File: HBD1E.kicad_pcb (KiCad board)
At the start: 2 copper layers, 73.1 x 50 mm, 62 parts, among them J1 Conn_01x08_Male, Q1 C3M0030090K, Q2 C3M0030090K, U1 UCC21520DW, U2 LM317_SOT-223, U3 3S7B-2424S3UP, U4 LM317_SOT-223, U5 3S7B-2424S3UP

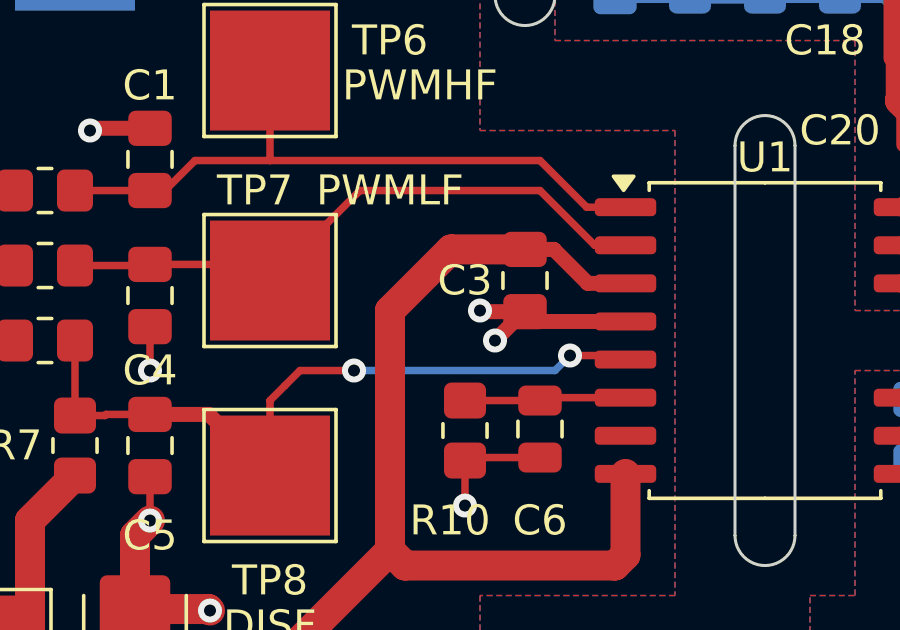
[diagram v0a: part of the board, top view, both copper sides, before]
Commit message: Added a pull-up resistor for dead time configuration.
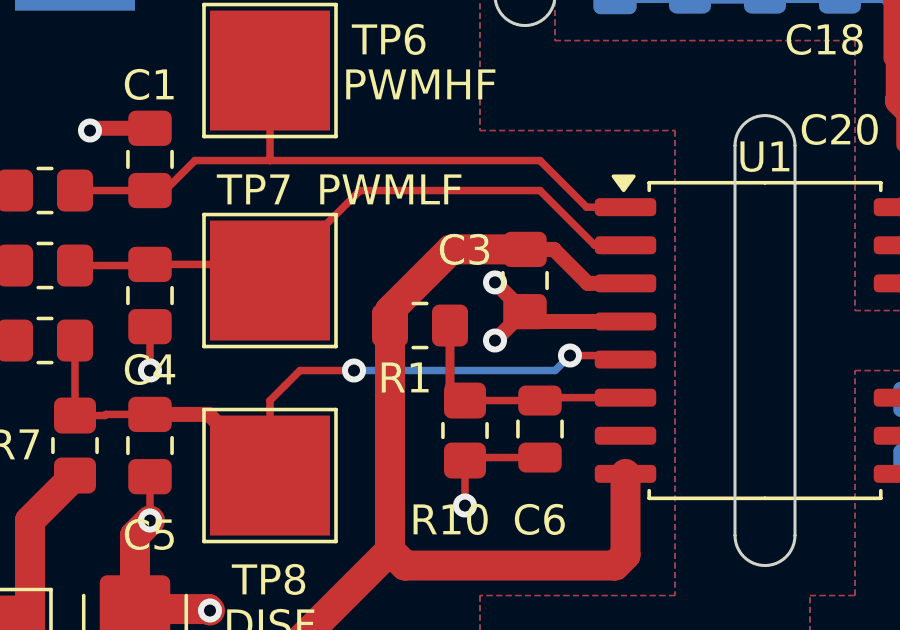
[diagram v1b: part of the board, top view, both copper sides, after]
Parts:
- added R1: 47, Resistor_SMD:R_0805_2012Metric_Pad1.20x1.40mm_HandSolder, F.Cu at (62.0, 64.0)
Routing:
- net Net-(U1-DT): track 5.39 -> 8.10 mm

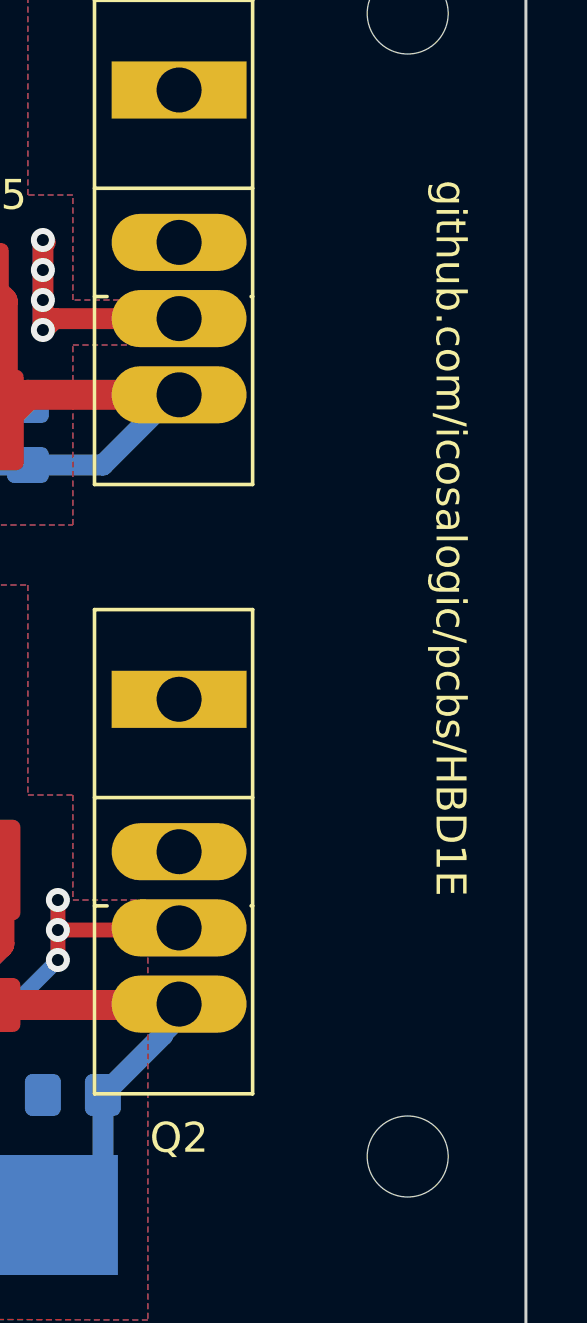
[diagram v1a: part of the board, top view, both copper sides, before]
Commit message: Fixed incorrect project location in PCB text object.
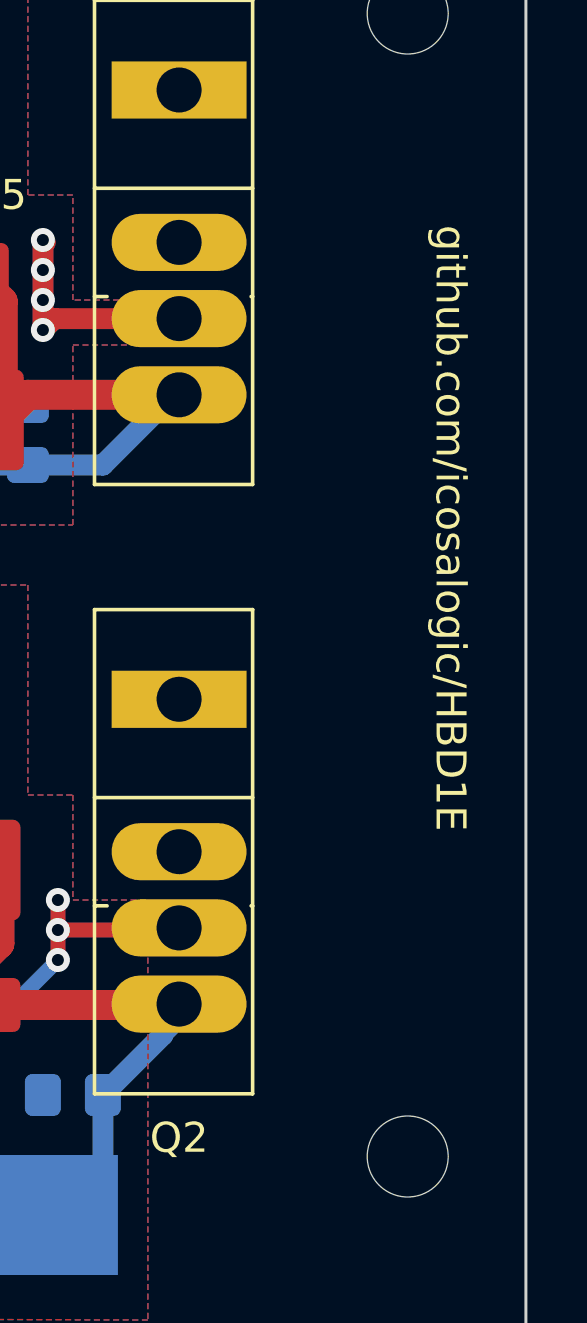
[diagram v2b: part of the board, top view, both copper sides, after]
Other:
- board text added: "github.com/icosalogic/HBD1E"
- board text removed: "github.com/icosalogic/pcbs/HBD1E"
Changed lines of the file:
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@@
 		(tags "resistor handsolder")
 		(property "Reference" "R1"
-			(at 0.5 -1.767767 360)
+			(at 0.5 -1.767767 0)
 			(layer "F.SilkS")
 			(effects
@@
 		)
 		(property "Value" "47"
-			(at 0.000001 1.65 360)
+			(at 0.000001 1.65 0)
 			(layer "F.Fab")
 			(hide yes)
@@
 		)
 		(fp_text user "${REFERENCE}"
-			(at 0 0 360)
+			(at 0 0 0)
 			(layer "F.Fab")
 			(hide yes)
@@
 		)
 	)
-	(gr_text "github.com/icosalogic/pcbs/HBD1E"
-		(at 108.5 52 270)
+	(gr_text "github.com/icosalogic/HBD1E"
+		(at 108.5 53.5 270)
 		(layer "F.SilkS")
 		(effects
